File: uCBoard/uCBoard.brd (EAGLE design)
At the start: 101.6 x 76.2 mm, 20 parts, among them X1 22-23-2041

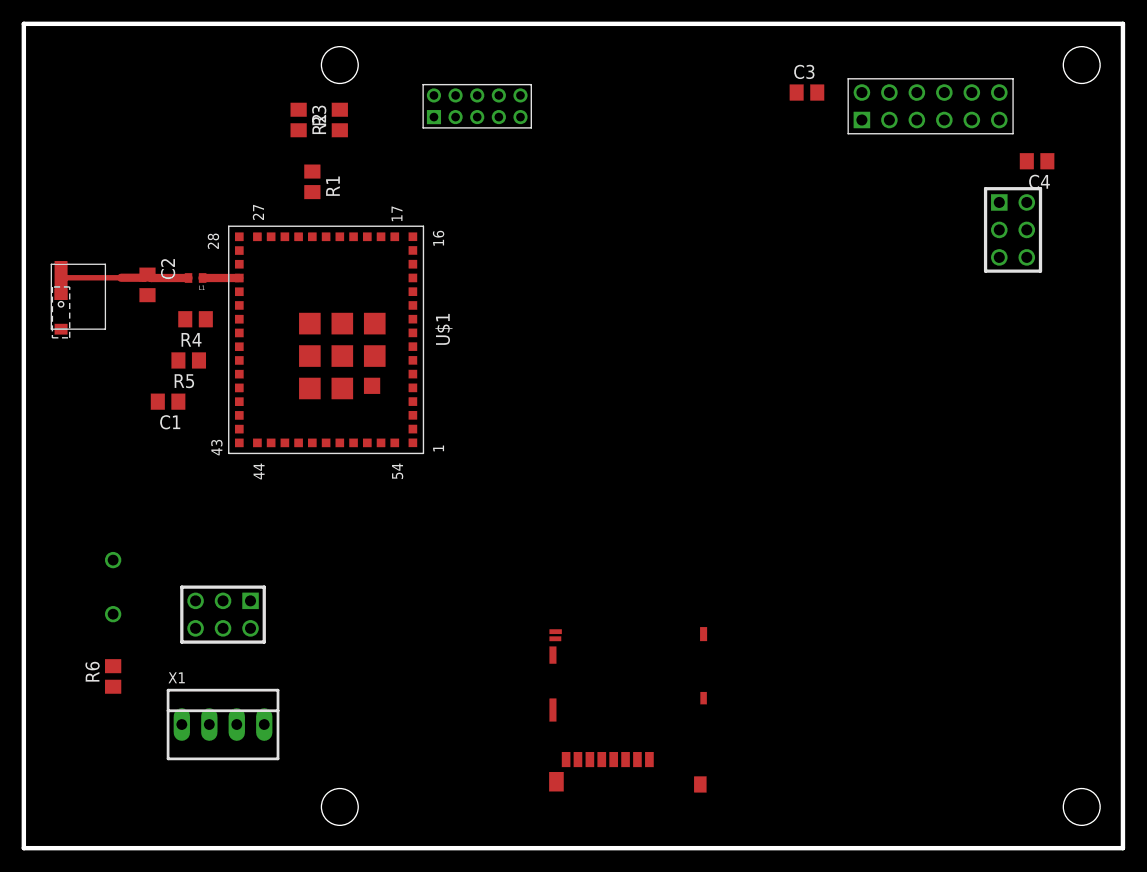
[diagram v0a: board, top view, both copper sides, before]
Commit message: Routed majority of uC Board
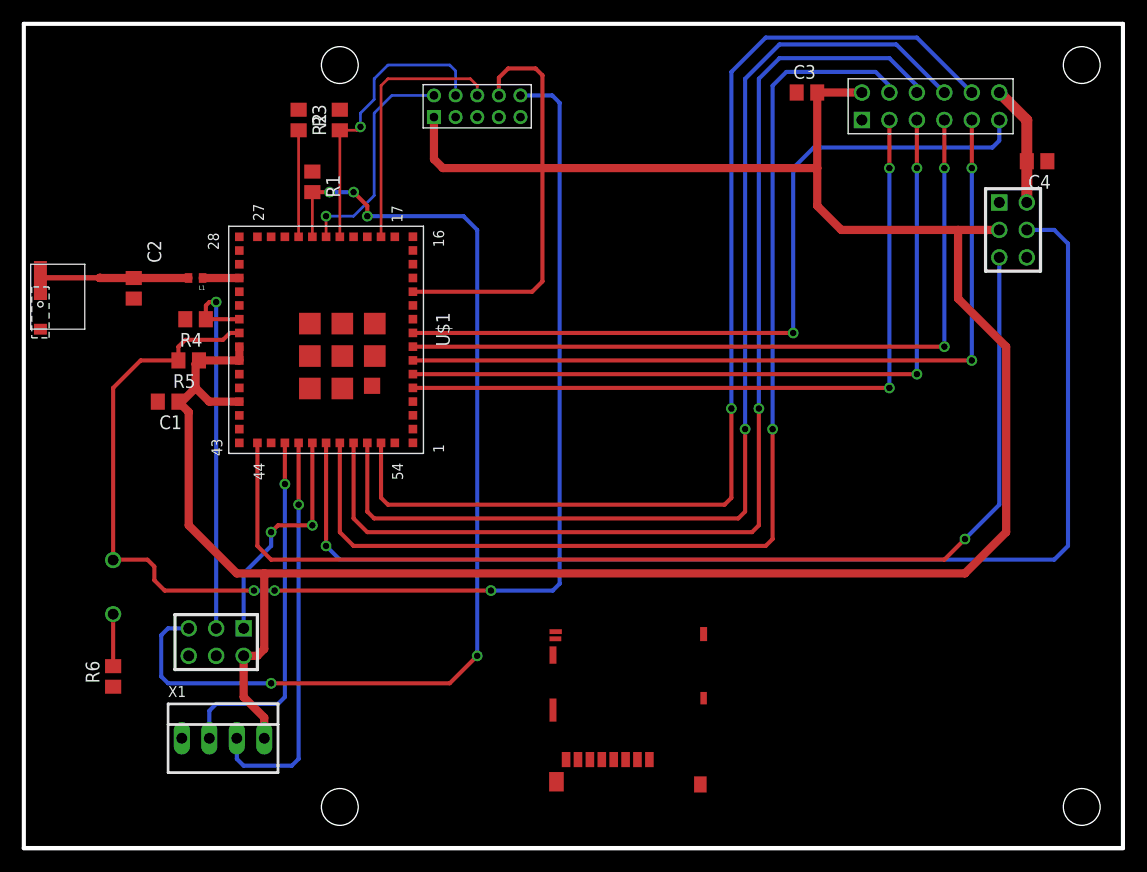
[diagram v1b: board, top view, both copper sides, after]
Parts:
- moved U$7 2.62 mm to (17.8, 19.1)
- moved U$2 1.91 mm to (0.64, 54.0)
- moved C2 1.31 mm to (10.2, 51.8)
- moved X1 1.27 mm to (18.4, 10.2)
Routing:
- net +3V3: track 0.00 -> 224.5 mm
- net N_RST: track 0.00 -> 122.3 mm, vias 0 -> 3
- net LSR_EN: track 0.00 -> 111.4 mm, vias 0 -> 1
- net TILT: track 0.00 -> 103.6 mm, vias 0 -> 1
- net BSY_Y: track 0.00 -> 103.6 mm, vias 0 -> 1
- net BSY_X: track 0.00 -> 103.4 mm, vias 0 -> 1
- net FLAG_X: track 0.00 -> 103.4 mm, vias 0 -> 1
- net FLAG_Y: track 0.00 -> 103.0 mm, vias 0 -> 1
- net SOP2: track 0.00 -> 97.9 mm, vias 0 -> 5
- net SPI_MISO: track 0.00 -> 73.9 mm, vias 0 -> 2
- net STNBY_RST: track 0.00 -> 72.4 mm, vias 0 -> 1
- net SPI_CLK: track 0.00 -> 70.1 mm, vias 0 -> 2
- net SPI_MOSI: track 0.00 -> 70.1 mm, vias 0 -> 2
- net SPI_CS: track 0.00 -> 68.8 mm, vias 0 -> 2
- net JTAG_TDI: track 0.00 -> 37.7 mm
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
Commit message: Added GND plane and fixed the SD card footprint
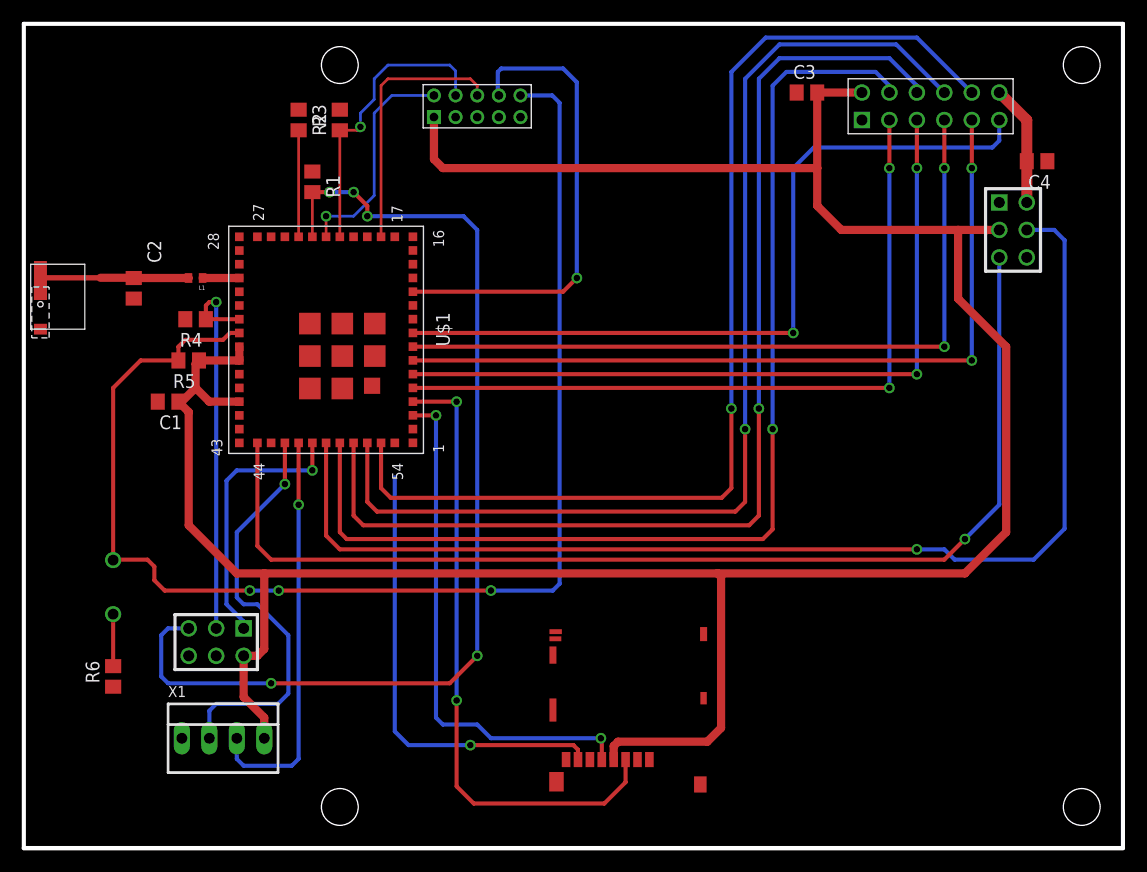
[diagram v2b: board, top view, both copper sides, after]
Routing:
- net SD_CMD: track 0.00 -> 58.8 mm, vias 0 -> 2
- net SD_CLK: track 0.00 -> 48.1 mm, vias 0 -> 2
- net SD_DATA: track 0.00 -> 42.0 mm, vias 0 -> 1
- net +3V3: track 224.5 -> 250.8 mm
- net JTAG_TDI: track 37.7 -> 43.9 mm, vias 0 -> 1
- net UART0_TX: track 33.5 -> 38.2 mm
- net CC_GPIO_03: track 21.6 -> 25.2 mm, vias 2 -> 1
- net LSR_EN: track 111.4 -> 109.5 mm
- net FLAG_Y: track 103.0 -> 101.4 mm
- net FLAG_X: track 103.4 -> 101.8 mm
- net BSY_Y: track 103.6 -> 102.4 mm
- net BSY_X: track 103.4 -> 102.4 mm
- net N$5: track 8.66 -> 8.15 mm
- added copper zone on layer 1, net GND
- added copper zone on layer 16, net GND

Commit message: Finished the uCBoard, added custom CAM processor, and created Gerber files
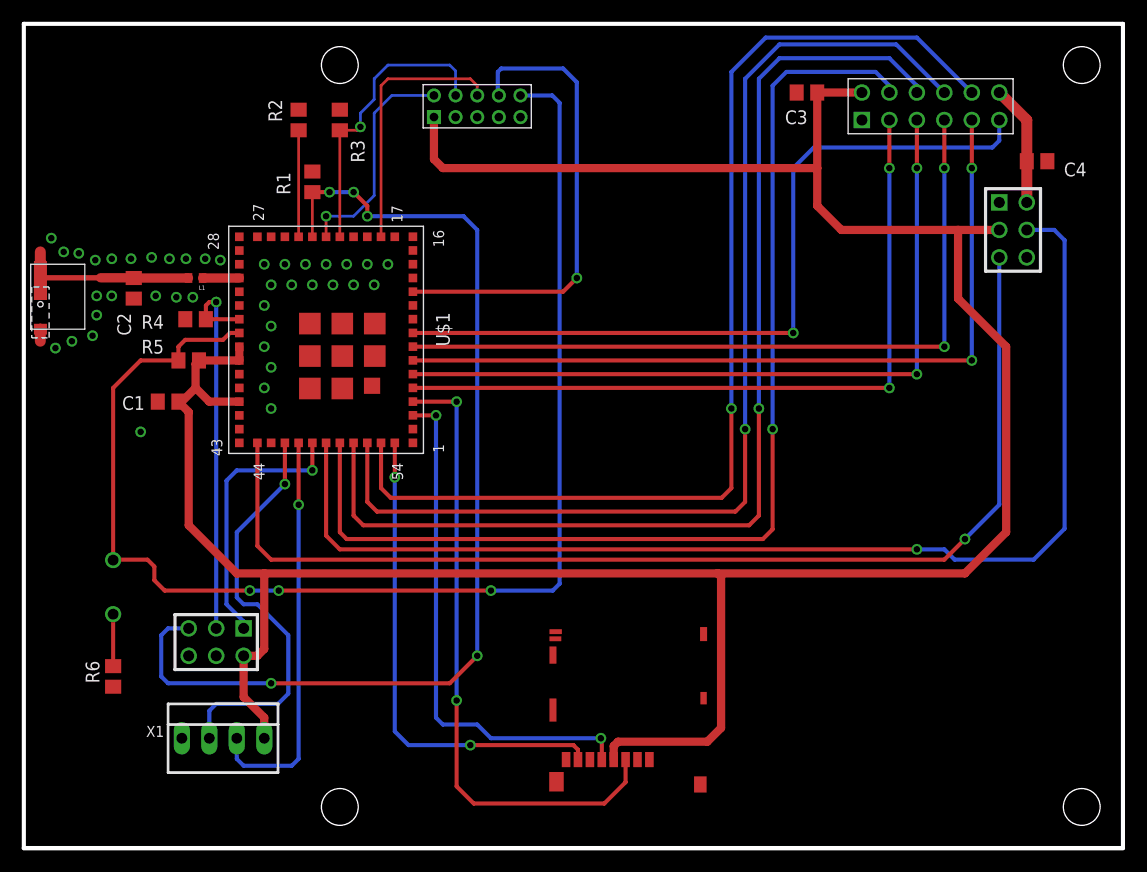
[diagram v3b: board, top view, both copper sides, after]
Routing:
- net SD_DATA: track 42.0 -> 45.2 mm, vias 1 -> 2
- net GND: track 0.00 -> 2.13 mm, vias 0 -> 40

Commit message: Committing gerber files
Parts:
- C1: device resistor:C0805 -> rcl:C1210
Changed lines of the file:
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@@
 </autorouter>
 <elements>
-<element name="C1" library="resistor" package="C0805" value="220uF" x="13.335" y="41.275" smashed="yes" rot="R180">
+<element name="C1" library="rcl" package="C1210" value="220uF" x="13.335" y="41.275" smashed="yes" rot="R180">
 <attribute name="NAME" x="11.176" y="41.783" size="1.27" layer="25" rot="R180"/>
 <attribute name="VALUE" x="14.605" y="43.815" size="1.27" layer="27" rot="R180"/>
@@
 <wire x1="38.735" y1="62.865" x2="73.34" y2="62.865" width="0.762" layer="1"/>
 <wire x1="16.19" y1="45.085" x2="19.92" y2="45.085" width="0.762" layer="1"/>
-<wire x1="14.285" y1="41.275" x2="14.605" y2="41.275" width="0.762" layer="1"/>
+<wire x1="14.735" y1="41.275" x2="14.605" y2="41.275" width="0.762" layer="1"/>
 <wire x1="14.605" y1="41.275" x2="15.875" y2="42.545" width="0.762" layer="1"/>
 <wire x1="15.875" y1="42.545" x2="15.875" y2="44.77" width="0.762" layer="1"/>
@@
 <wire x1="19.685" y1="25.4" x2="15.24" y2="29.845" width="0.762" layer="1"/>
 <wire x1="15.24" y1="29.845" x2="15.24" y2="40.32" width="0.762" layer="1"/>
-<wire x1="15.24" y1="40.32" x2="14.285" y2="41.275" width="0.762" layer="1"/>
+<wire x1="15.24" y1="40.32" x2="14.735" y2="41.275" width="0.762" layer="1"/>
 <wire x1="20.32" y1="17.78" x2="21.59" y2="17.78" width="0.762" layer="1"/>
 <wire x1="21.59" y1="17.78" x2="22.225" y2="18.415" width="0.762" layer="1"/>

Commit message: Fixing labeling on the uC board so that SPI is correct
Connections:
- net SPI_CLK: now also U$1.P5, U$6.3; no longer U$1.P8, U$6.7
- net SPI_CS: now also U$1.P8, U$6.7; no longer U$1.P5, U$6.3
- net SPI_MISO: now also U$1.P6, U$6.5; no longer U$1.P7, U$6.9
- net SPI_MOSI: now also U$1.P7, U$6.9; no longer U$1.P6, U$6.5
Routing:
- net SPI_MISO: track 73.9 -> 70.1 mm
- net SPI_MOSI: track 70.1 -> 73.9 mm
- net SPI_CS: track 68.8 -> 70.1 mm
- net SPI_CLK: track 70.1 -> 68.8 mm
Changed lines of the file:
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@@
 <wire x1="92.7125" y1="67.3075" x2="90.17" y2="69.85" width="1.016" layer="1"/>
 </signal>
-<signal name="SPI_CS">
+<signal name="SPI_CLK">
 <contactref element="U$6" pad="3"/>
 <contactref element="U$1" pad="P5"/>
@@
 <wire x1="35.97" y1="47.625" x2="35.965" y2="47.63" width="0.381" layer="1"/>
 </signal>
-<signal name="SPI_MISO">
+<signal name="SPI_MOSI">
 <contactref element="U$6" pad="9"/>
 <contactref element="U$1" pad="P7"/>
@@
 <wire x1="35.97" y1="45.085" x2="35.965" y2="45.09" width="0.381" layer="1"/>
 </signal>
-<signal name="SPI_CLK">
+<signal name="SPI_CS">
 <contactref element="U$6" pad="7"/>
 <contactref element="U$1" pad="P8"/>
@@
 <wire x1="85.09" y1="46.355" x2="35.97" y2="46.355" width="0.381" layer="1"/>
 <wire x1="35.97" y1="46.355" x2="35.965" y2="46.36" width="0.381" layer="1"/>
-</signal>
-<signal name="SPI_MOSI">
-<contactref element="U$6" pad="5"/>
-<contactref element="U$1" pad="P6"/>
-<wire x1="82.55" y1="67.31" x2="82.55" y2="62.865" width="0.381" layer="1"/>
-<via x="82.55" y="62.865" extent="1-16" drill="0.6"/>
-<wire x1="82.55" y1="62.865" x2="82.55" y2="43.815" width="0.381" layer="16"/>
-<via x="82.55" y="43.815" extent="1-16" drill="0.6"/>
-<wire x1="82.55" y1="43.815" x2="35.97" y2="43.815" width="0.381" layer="1"/>
-<wire x1="35.97" y1="43.815" x2="35.965" y2="43.82" width="0.381" layer="1"/>
 </signal>
 <signal name="UART0_TX">
@@
 <wire x1="38.1" y1="12.065" x2="38.1" y2="40.005" width="0.381" layer="16"/>
 </signal>
+<signal name="SPI_MISO">
+<contactref element="U$1" pad="P6"/>
+<contactref element="U$6" pad="5"/>
+<wire x1="82.55" y1="67.31" x2="82.55" y2="62.865" width="0.381" layer="1"/>
+<via x="82.55" y="62.865" extent="1-16" drill="0.6"/>
+<wire x1="82.55" y1="62.865" x2="82.55" y2="43.815" width="0.381" layer="16"/>
+<via x="82.55" y="43.815" extent="1-16" drill="0.6"/>
+<wire x1="82.55" y1="43.815" x2="35.97" y2="43.815" width="0.381" layer="1"/>
+<wire x1="35.97" y1="43.815" x2="35.965" y2="43.82" width="0" layer="19" extent="1-1"/>
+</signal>
 </signals>
